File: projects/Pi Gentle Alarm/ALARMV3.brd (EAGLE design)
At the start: 65 x 56 mm, 6 parts, among them IC1 7805T, X1 RASPI_BOARD_B+_E0

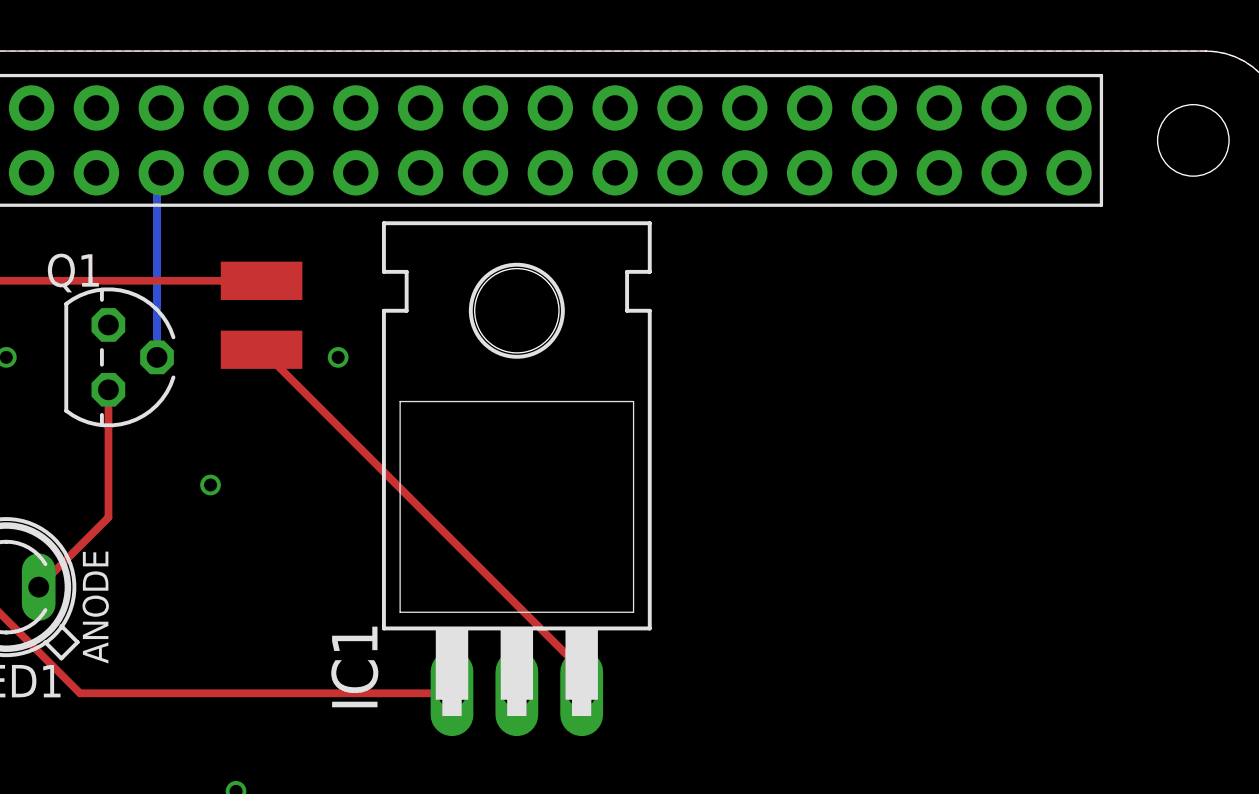
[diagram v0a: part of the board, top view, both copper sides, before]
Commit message: Added a button for turning off the alarm
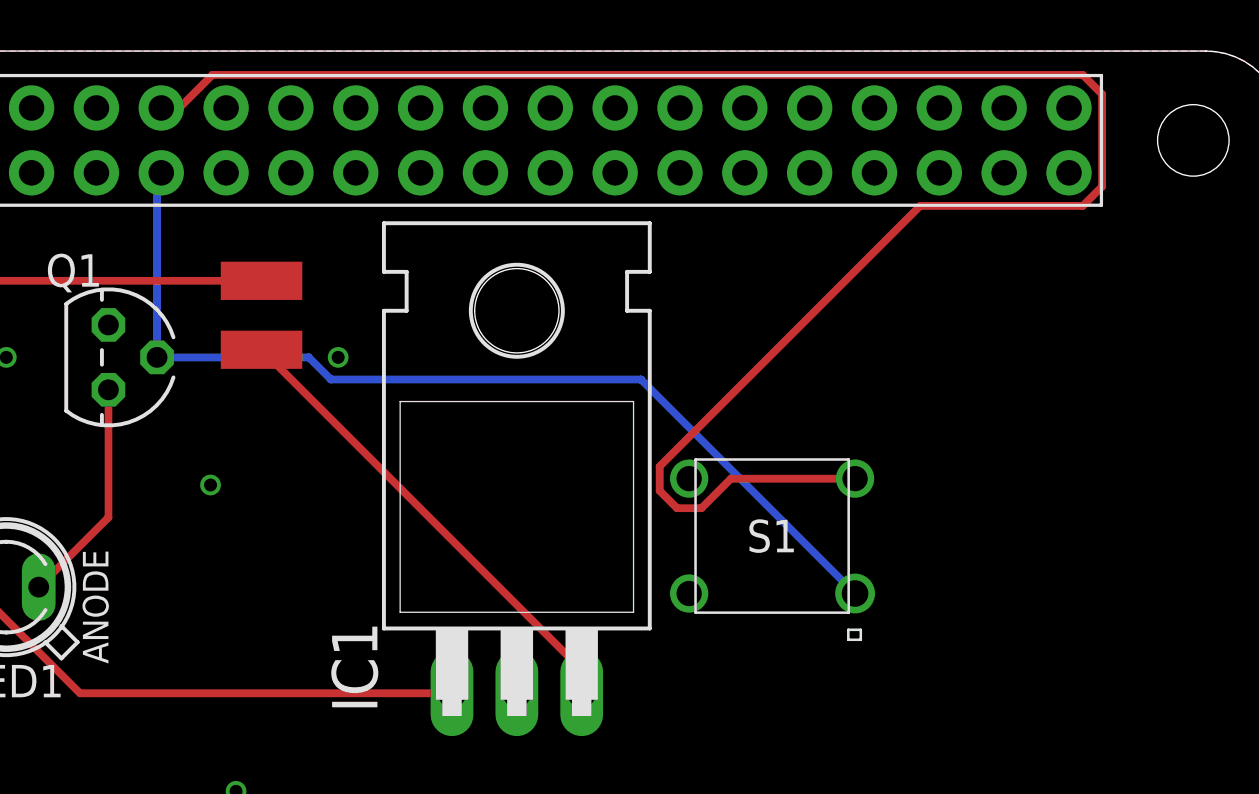
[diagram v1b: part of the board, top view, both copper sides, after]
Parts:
- added S1: 2-1825910-7, SamacSys_Parts:TE-6MM-TACT-SWITCH
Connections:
- new net N$3: S1.3, X1.12
- net GPIO17: now also S1.1
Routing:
- net N$3: track 0.00 -> 72.6 mm
- net GPIO17: track 7.30 -> 38.5 mm
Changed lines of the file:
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@@
 </element>
 <element name="F1" library="Test" package="MF-MSMF260-2" value="" x="25" y="47" smashed="yes" rot="R90"/>
+<element name="S1" library="SamacSys_Parts" package="TE-6MM-TACT-SWITCH" value="2-1825910-7" x="45" y="37" smashed="yes">
+<attribute name="DESCRIPTION" value="Black Tactile Tactile Switch, SPST 50 mA 9.4mm" x="45" y="37" size="1.778" layer="27" display="off"/>
+<attribute name="HEIGHT" value="mm" x="45" y="37" size="1.778" layer="27" display="off"/>
+<attribute name="MANUFACTURER_NAME" value="TE Connectivity" x="45" y="37" size="1.778" layer="27" display="off"/>
+<attribute name="MANUFACTURER_PART_NUMBER" value="2-1825910-7" x="45" y="37" size="1.778" layer="27" display="off"/>
+<attribute name="MOUSER_PART_NUMBER" value="506-2-1825910-7" x="45" y="37" size="1.778" layer="27" display="off"/>
+<attribute name="MOUSER_PRICE-STOCK" value="https://www.mouser.com/Search/Refine.aspx?Keyword=506-2-1825910-7" x="45" y="37" size="1.778" layer="27" display="off"/>
+<attribute name="NAME" x="45" y="37" size="1.27" layer="25" align="center"/>
+<attribute name="VALUE" x="45" y="37" size="1.27" layer="27" align="center"/>
+</element>
 </elements>
 <signals>
@@
 <wire x1="20.905" y1="44" x2="20.905" y2="51.065" width="0.3048" layer="16"/>
 <wire x1="20.905" y1="51.065" x2="21.07" y2="51.23" width="0.3048" layer="16"/>
+<contactref element="S1" pad="1"/>
+<wire x1="26.850525" y1="44" x2="20.905" y2="44" width="0.3048" layer="16"/>
+<wire x1="48.25" y1="34.75" x2="39.8664" y2="43.1336" width="0.3048" layer="16"/>
+<wire x1="39.8664" y1="43.1336" x2="27.716925" y2="43.1336" width="0.3048" layer="16"/>
+<wire x1="27.716925" y1="43.1336" x2="26.850525" y2="44" width="0.3048" layer="16"/>
 </signal>
 <signal name="N$6">
@@
 <wire x1="37.54" y1="31.76" x2="37.54" y2="30.84" width="0.3048" layer="1"/>
 </signal>
+<signal name="N$3">
+<contactref element="S1" pad="3"/>
+<contactref element="X1" pad="12"/>
+<wire x1="42.229" y1="38.0936" x2="41.271" y2="38.0936" width="0.3048" layer="1"/>
+<wire x1="57.166575" y1="49.9346" x2="57.9254" y2="50.693425" width="0.3048" layer="1"/>
+<wire x1="57.9254" y1="54.306575" x2="57.166575" y2="55.0654" width="0.3048" layer="1"/>
+<wire x1="48.25" y1="39.25" x2="43.3854" y2="39.25" width="0.3048" layer="1"/>
+<wire x1="43.3854" y1="39.25" x2="42.229" y2="38.0936" width="0.3048" layer="1"/>
+<wire x1="57.9254" y1="50.693425" x2="57.9254" y2="54.306575" width="0.3048" layer="1"/>
+<wire x1="57.166575" y1="55.0654" x2="23.073425" y2="55.0654" width="0.3048" layer="1"/>
+<wire x1="41.271" y1="38.0936" x2="40.5936" y2="38.771" width="0.3048" layer="1"/>
+<wire x1="40.5936" y1="38.771" x2="40.5936" y2="39.729" width="0.3048" layer="1"/>
+<wire x1="40.5936" y1="39.729" x2="50.7992" y2="49.9346" width="0.3048" layer="1"/>
+<wire x1="50.7992" y1="49.9346" x2="57.166575" y2="49.9346" width="0.3048" layer="1"/>
+<wire x1="21.778025" y1="53.77" x2="21.07" y2="53.77" width="0.3048" layer="1"/>
+<wire x1="23.073425" y1="55.0654" x2="21.778025" y2="53.77" width="0.3048" layer="1"/>
+</signal>
 </signals>

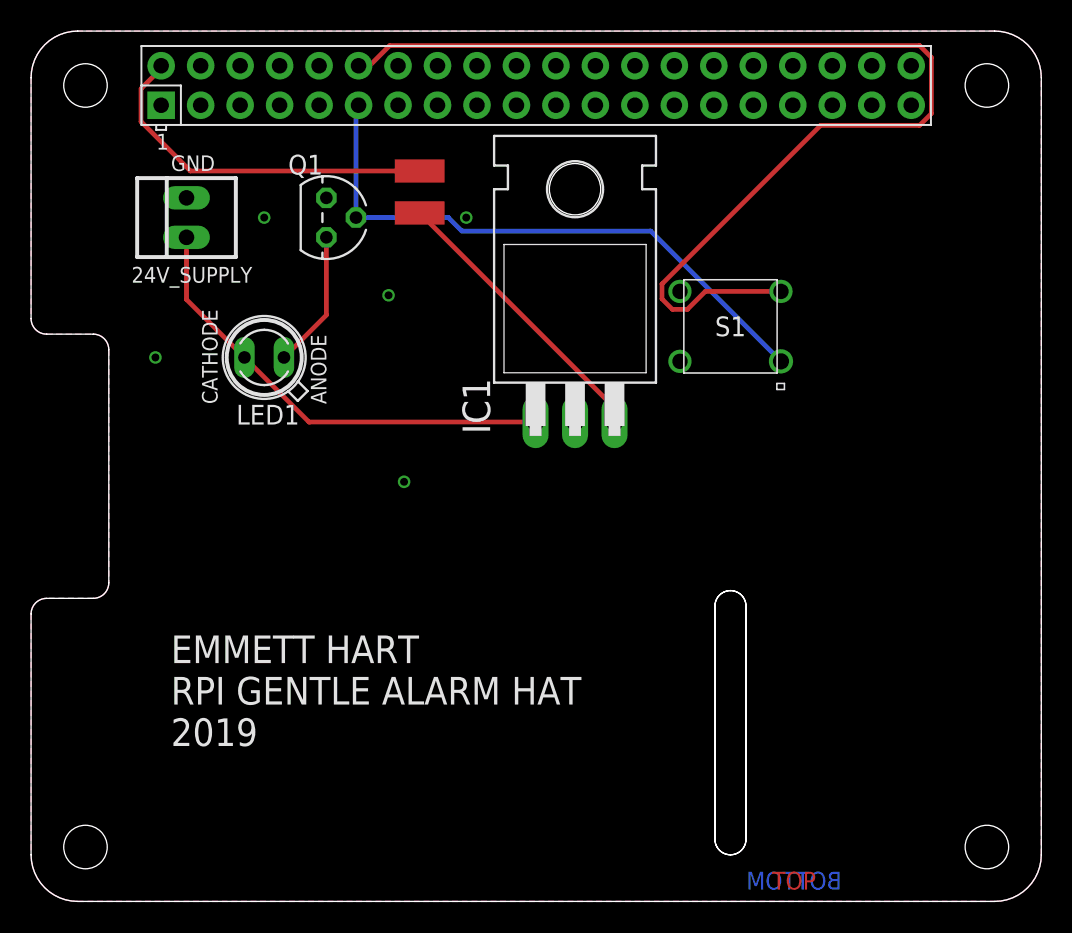
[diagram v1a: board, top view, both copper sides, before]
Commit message: Satisfied dependancies
Voltage regulator needed capacitors
Changed shut-off button
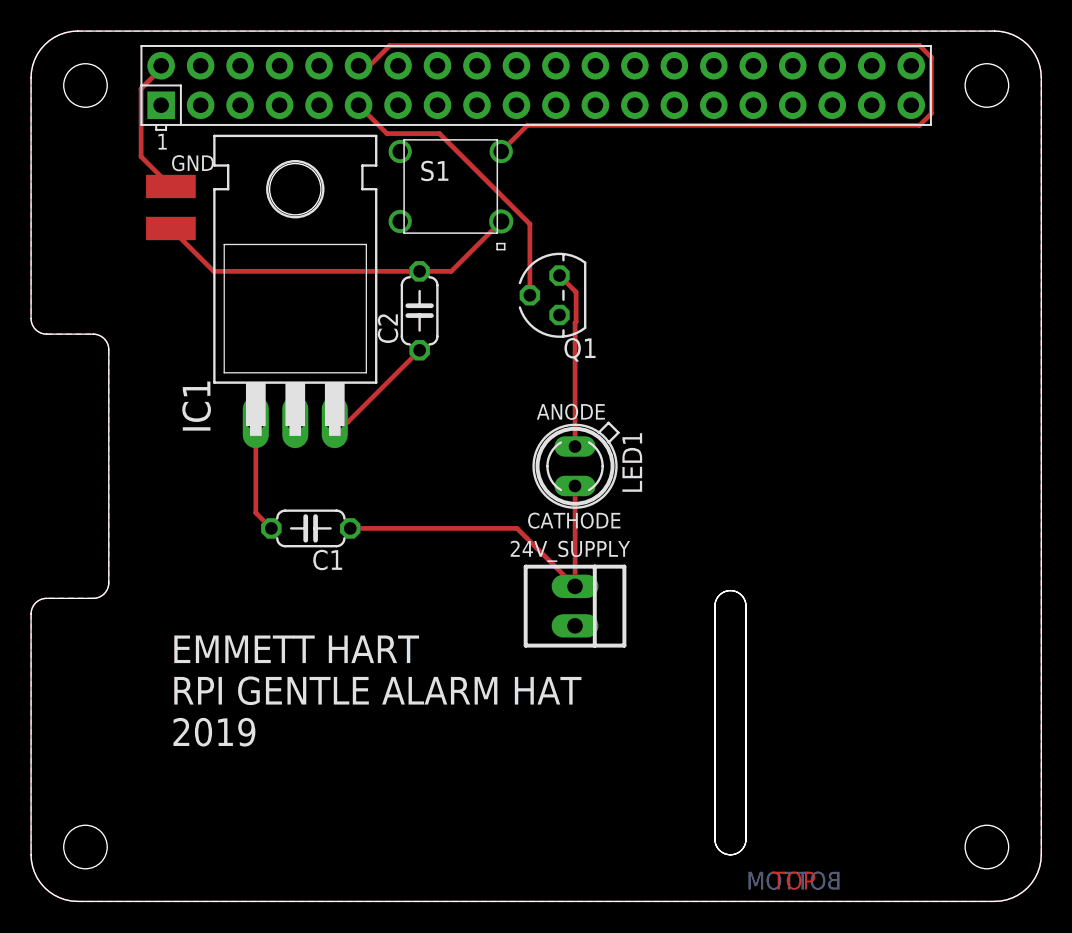
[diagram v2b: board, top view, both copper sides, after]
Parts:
- added C1: 22uf, adafruit:C050-024X044
- added C2: .1uf, adafruit:C050-024X044
- moved 24V_SUPPLY 35.4 mm to (35.0, 19.0), turned to 270 degrees
- moved LED1 21.2 mm to (35.0, 28.0), turned to 270 degrees
- moved S1 20.1 mm to (27.0, 46.0)
- moved IC1 18.0 mm to (17.0, 41.0)
- moved F1 16.0 mm to (9.00, 46.0)
- moved Q1 15.8 mm to (34.0, 39.0), turned to 90 degrees
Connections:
- new net N$4: C1.2, IC1.1
- new net N$5: C2.1, IC1.3
- net GPIO17: no longer S1.1
- net N$2: now also C2.2, S1.1; no longer IC1.3
- net VCC: now also C1.1; no longer IC1.1
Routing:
- net GPIO17: track 38.5 -> 18.8 mm
- net N$1: track 23.4 -> 9.10 mm
- net N$5: track 0.00 -> 7.37 mm
- net VCC: track 29.7 -> 22.5 mm
- net N$4: track 0.00 -> 7.25 mm
- net N$2: track 18.7 -> 23.7 mm
- net N$6: track 8.86 -> 11.5 mm
- net N$3: track 72.6 -> 70.0 mm

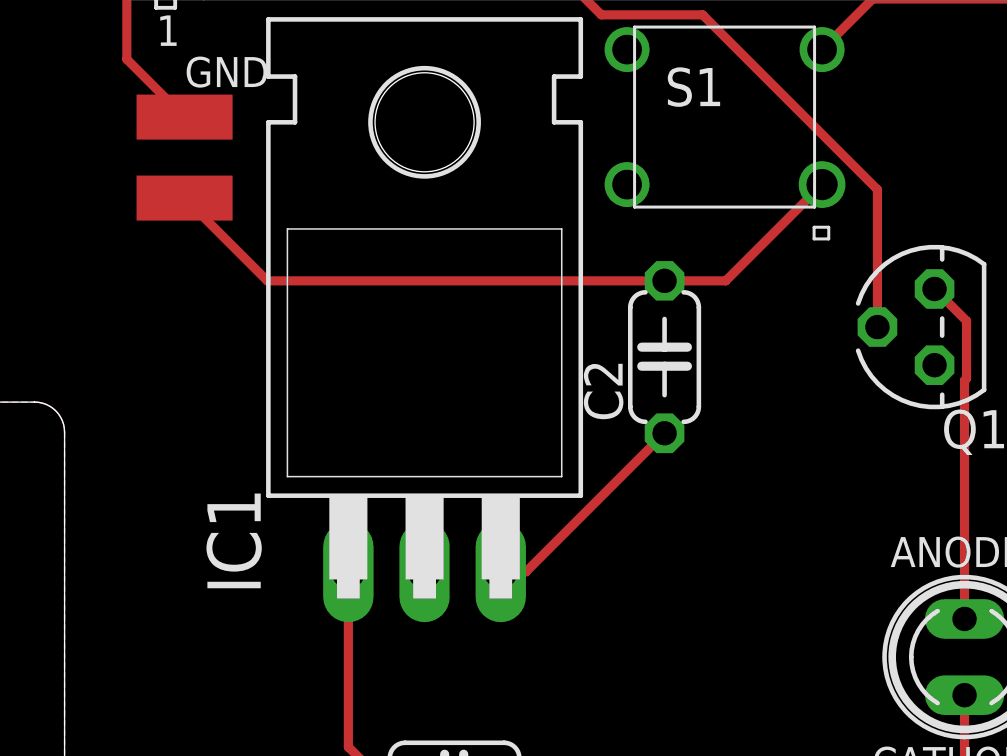
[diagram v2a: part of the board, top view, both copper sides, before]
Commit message: Removed extra components
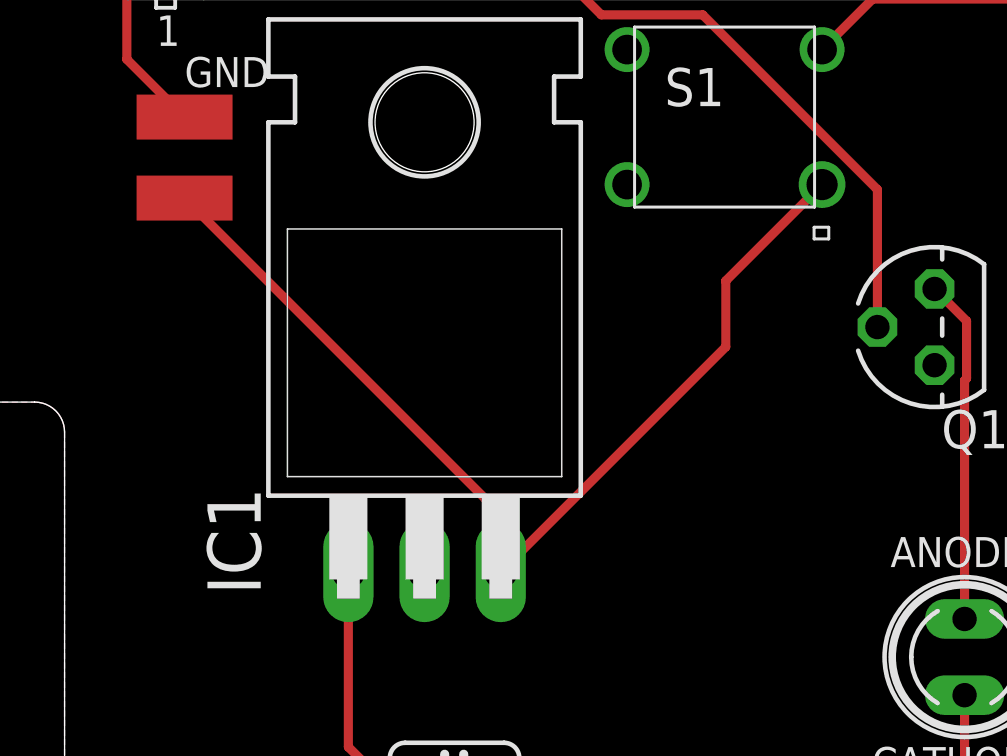
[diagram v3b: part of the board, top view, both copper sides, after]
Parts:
- removed C2: .1uf, adafruit:C050-024X044
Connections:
- removed net N$2: C2.2, F1.P$2, S1.1
- net N$5: now also F1.P$2, S1.1; no longer C2.1
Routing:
- net N$5: track 7.37 -> 34.2 mm
- net N$2: track 23.7 -> 0.00 mm
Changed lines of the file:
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@@
 <attribute name="VALUE" x="20.159" y="26.667" size="1.27" layer="27" ratio="10" rot="R180"/>
-</element>
-<element name="C2" library="adafruit" library_urn="urn:adsk.eagle:library:420" package="C050-024X044" package3d_urn="urn:adsk.eagle:package:6240356/1" value=".1uf" x="25" y="38" smashed="yes" rot="R90">
-<attribute name="NAME" x="23.603" y="35.841" size="1.27" layer="25" ratio="10" rot="R90"/>
-<attribute name="VALUE" x="27.667" y="35.841" size="1.27" layer="27" ratio="10" rot="R90"/>
 </element>
 </elements>
@@
 <wire x1="7.0746" y1="47.9254" x2="9" y2="46" width="0.3048" layer="1"/>
 </signal>
-<signal name="N$2">
-<contactref element="F1" pad="P$2"/>
-<contactref element="S1" pad="1"/>
-<contactref element="C2" pad="2"/>
-<wire x1="9" y1="43.3" x2="11.76" y2="40.54" width="0.3048" layer="1"/>
-<wire x1="11.76" y1="40.54" x2="25" y2="40.54" width="0.3048" layer="1"/>
-<wire x1="25" y1="40.54" x2="27.04" y2="40.54" width="0.3048" layer="1"/>
-<wire x1="27.04" y1="40.54" x2="30.25" y2="43.75" width="0.3048" layer="1"/>
-</signal>
 <signal name="N$3">
 <contactref element="S1" pad="3"/>
@@
 <signal name="N$5">
 <contactref element="IC1" pad="3"/>
-<contactref element="C2" pad="1"/>
-<wire x1="19.54" y1="30.84" x2="20.38" y2="30.84" width="0.3048" layer="1"/>
-<wire x1="20.38" y1="30.84" x2="25" y2="35.46" width="0.3048" layer="1"/>
+<contactref element="F1" pad="P$2"/>
+<contactref element="S1" pad="1"/>
+<wire x1="30.25" y1="43.75" x2="27.04" y2="40.54" width="0.3048" layer="1"/>
+<wire x1="9" y1="43.3" x2="19.54" y2="32.76" width="0.3048" layer="1"/>
+<wire x1="19.54" y1="32.76" x2="19.54" y2="30.84" width="0.3048" layer="1"/>
+<wire x1="27.04" y1="40.54" x2="27.04" y2="38.34" width="0.3048" layer="1"/>
+<wire x1="27.04" y1="38.34" x2="19.54" y2="30.84" width="0.3048" layer="1"/>
 </signal>
 </signals>

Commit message: Added a part
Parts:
- removed Q1: (no value), transistors:TO-92
- added IC2: STP14NF10, SamacSys_Parts:TO270P460X1020X2008-3P
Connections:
- net GND: now also IC2.3; no longer Q1.1
- net GPIO17: now also IC2.1; no longer Q1.2
- net N$6: now also IC2.2; no longer Q1.3
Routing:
- net GPIO17: track 18.8 -> 19.3 mm
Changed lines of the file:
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@@
 <?xml version="1.0" encoding="utf-8"?>
 <!DOCTYPE eagle SYSTEM "eagle.dtd">
-<eagle version="9.5.0">
+<eagle version="9.5.1">
 <drawing>
 <settings>
-<setting alwaysvectorfont="no"/>
+<setting alwaysvectorfont="yes"/>
 <setting keepoldvectorfont="yes"/>
 <setting verticaltext="up"/>
@@
 <attribute name="VALUE" x="29.92" y="21.54" size="1.016" layer="27" ratio="10" rot="R270"/>
 </element>
-<element name="Q1" library="transistors" package="TO-92" value="" x="34" y="39" smashed="yes" rot="R90">
-<attribute name="MF" value="" x="34" y="39" size="1.778" layer="27" rot="R90" display="off"/>
-<attribute name="MPN" value="2N7000." x="34" y="39" size="1.778" layer="27" rot="R90" display="off"/>
-<attribute name="NAME" x="36.46" y="36.23" size="1.27" layer="25" ratio="10" rot="R180"/>
-<attribute name="OC_NEWARK" value="26AC6371" x="34" y="39" size="1.778" layer="27" rot="R90" display="off"/>
-<attribute name="VALUE" x="35.27" y="42.175" size="1.27" layer="27" ratio="10" rot="R90"/>
-</element>
 <element name="LED1" library="adafruit" library_urn="urn:adsk.eagle:library:420" package="SFH482" package3d_urn="urn:adsk.eagle:package:6240546/1" value="" x="35" y="28" smashed="yes" rot="R270">
 <attribute name="MF" value="" x="35" y="28" size="1.778" layer="27" rot="R270" display="off"/>
@@
 <attribute name="NAME" x="20.159" y="22.603" size="1.27" layer="25" ratio="10" rot="R180"/>
 <attribute name="VALUE" x="20.159" y="26.667" size="1.27" layer="27" ratio="10" rot="R180"/>
+</element>
+<element name="IC2" library="SamacSys_Parts" package="TO270P460X1020X2008-3P" value="STP14NF10" x="37" y="43" smashed="yes" rot="R270">
+<attribute name="DESCRIPTION" value="STP14NF10, N-channel MOSFET Transistor 15 A 100 V, 3-Pin TO-220" x="37" y="43" size="1.778" layer="27" rot="R270" display="off"/>
+<attribute name="HEIGHT" value="4.6mm" x="37" y="43" size="1.778" layer="27" rot="R270" display="off"/>
+<attribute name="MANUFACTURER_NAME" value="STMicroelectronics" x="37" y="43" size="1.778" layer="27" rot="R270" display="off"/>
+<attribute name="MANUFACTURER_PART_NUMBER" value="STP14NF10" x="37" y="43" size="1.778" layer="27" rot="R270" display="off"/>
+<attribute name="MOUSER_PART_NUMBER" value="511-STP14NF10" x="37" y="43" size="1.778" layer="27" rot="R270" display="off"/>
+<attribute name="MOUSER_PRICE-STOCK" value="https://www.mouser.com/Search/Refine.aspx?Keyword=511-STP14NF10" x="37" y="43" size="1.778" layer="27" rot="R270" display="off"/>
+<attribute name="NAME" x="35" y="43" size="1.27" layer="25" rot="R270" align="center"/>
+<attribute name="VALUE" x="37" y="43" size="1.27" layer="27" rot="R270" align="center"/>
 </element>
 </elements>
@@
 <contactref element="X1" pad="6"/>
 <contactref element="24V_SUPPLY" pad="2"/>
-<contactref element="Q1" pad="1"/>
 <contactref element="IC1" pad="2"/>
+<contactref element="IC2" pad="3"/>
 </signal>
 <signal name="3V3">
@@
 </signal>
 <signal name="GPIO17">
-<contactref element="Q1" pad="2"/>
 <contactref element="X1" pad="11"/>
-<wire x1="21.07" y1="51.23" x2="22.8936" y2="49.4064" width="0.3048" layer="1"/>
-<wire x1="32.095" y1="43.582825" x2="32.095" y2="39" width="0.3048" layer="1"/>
-<wire x1="22.8936" y1="49.4064" x2="26.271425" y2="49.4064" width="0.3048" layer="1"/>
-<wire x1="26.271425" y1="49.4064" x2="32.095" y2="43.582825" width="0.3048" layer="1"/>
+<contactref element="IC2" pad="1"/>
+<wire x1="21.07" y1="51.23" x2="21.778025" y2="51.23" width="0.3048" layer="1"/>
+<wire x1="32.9064" y1="47.0936" x2="37" y2="43" width="0.3048" layer="1"/>
+<wire x1="21.778025" y1="51.23" x2="23.073425" y2="49.9346" width="0.3048" layer="1"/>
+<wire x1="29.771" y1="47.0936" x2="32.9064" y2="47.0936" width="0.3048" layer="1"/>
+<wire x1="23.073425" y1="49.9346" x2="26.93" y2="49.9346" width="0.3048" layer="1"/>
+<wire x1="26.93" y1="49.9346" x2="29.771" y2="47.0936" width="0.3048" layer="1"/>
 </signal>
 <signal name="N$6">
-<contactref element="Q1" pad="3"/>
 <contactref element="LED1" pad="A"/>
-<wire x1="35.0668" y1="37.2881125" x2="35" y2="37.2213125" width="0.3048" layer="1"/>
-<wire x1="35" y1="37.2213125" x2="35" y2="29.27" width="0.3048" layer="1"/>
-<wire x1="34" y1="40.27" x2="35.0668" y2="39.2032" width="0.3048" layer="1"/>
-<wire x1="35.0668" y1="39.2032" x2="35.0668" y2="37.2881125" width="0.3048" layer="1"/>
+<wire x1="35" y1="37.2213125" x2="35" y2="37" width="0.3048" layer="1"/>
+<contactref element="IC2" pad="2"/>
+<wire x1="35" y1="37" x2="35" y2="29.27" width="0.3048" layer="1"/>
+<wire x1="35" y1="37.2213125" x2="35" y2="38.3" width="0.3048" layer="1"/>
+<wire x1="35" y1="38.3" x2="37" y2="40.3" width="0.3048" layer="1"/>
 </signal>
 <signal name="N$1">
